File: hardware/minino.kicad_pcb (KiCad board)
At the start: 2 copper layers, 80 x 107.5 mm, 54 parts, among them J1 OLED, J2 GPS, J3 Battery, J5 Micro_SD_Card_Det, P1 USB_C_Plug_USB2.0, Q1 DMG3415U-7, Q2 MMBT2222A, SW1 ON, SW2 LEFT, SW3 RIGTH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

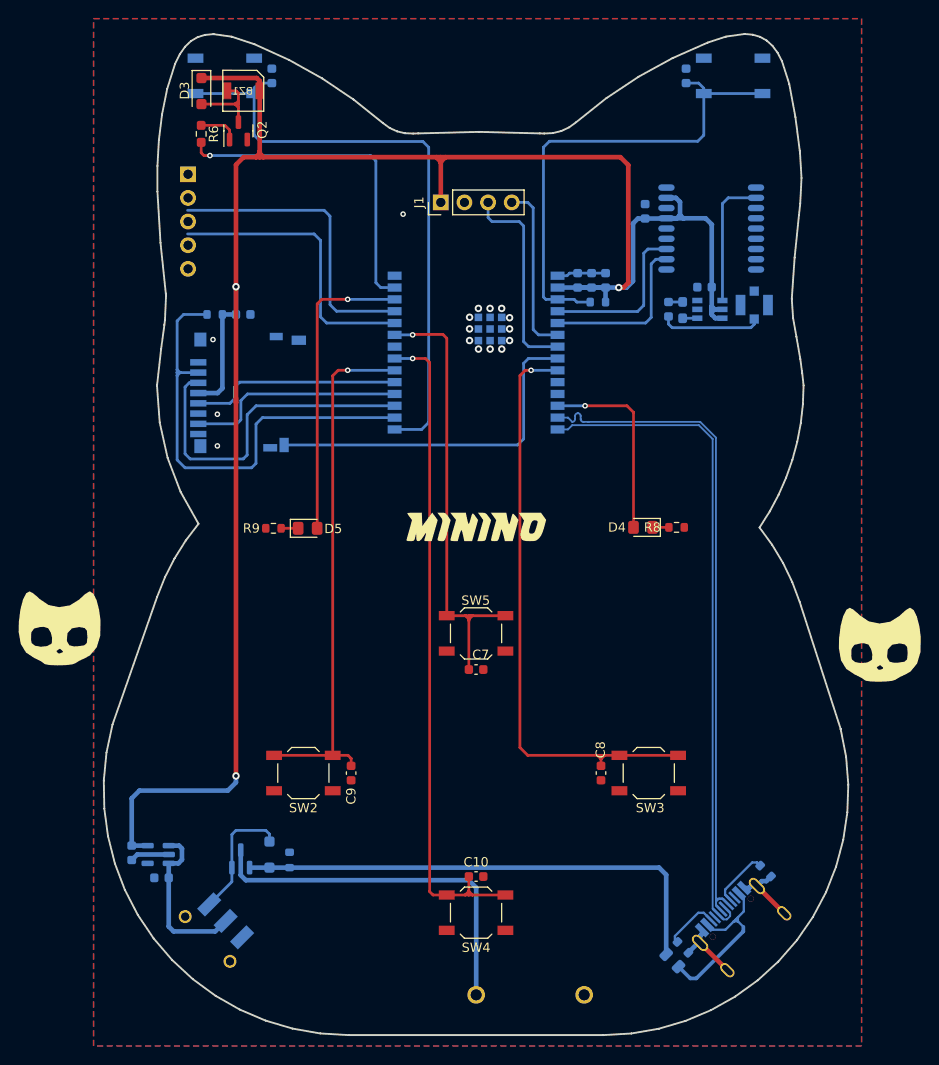
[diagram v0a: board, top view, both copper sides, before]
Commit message: Uart header placed
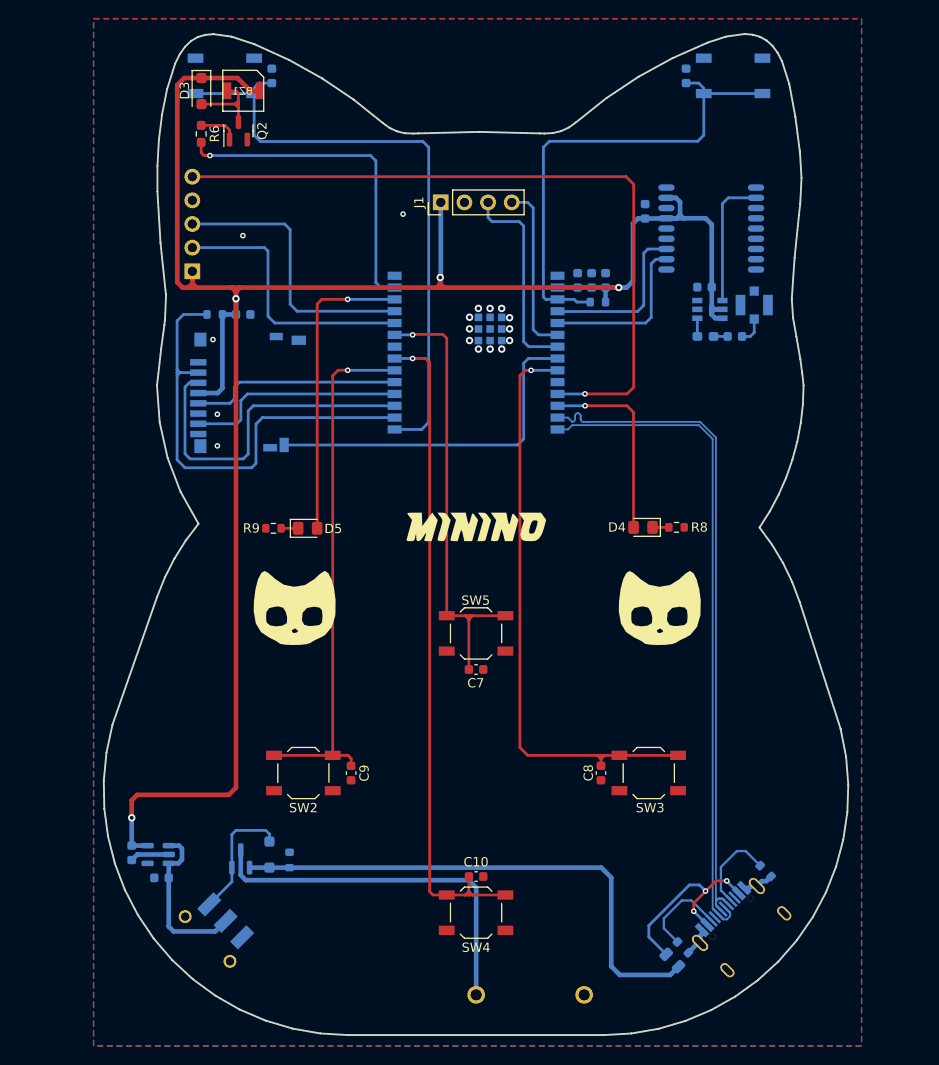
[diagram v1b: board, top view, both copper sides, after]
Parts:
- moved G*** 25.3 mm to (71.2, 83.1)
- moved G*** 24.0 mm to (110.4, 83.1)
- moved J2 10.4 mm to (60.3, 46.9), turned to 0 degrees
- moved C1 7.71 mm to (118.6, 53.9), turned to 0 degrees
- moved L1 3.75 mm to (115.4, 53.9), turned to 0 degrees
- moved G*** 0.59 mm to (72.1, 37.1)
- moved G*** 0.59 mm to (72.7, 45.9)
- turned F1 to -45 degrees
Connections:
- J2 pad 2: /TX -> /RX
- J2 pad 3: /RX -> /TX
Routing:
- net /DIO11: track 0.00 -> 78.0 mm, vias 0 -> 1
- net GND: track 24.4 -> 10.8 mm, vias 16 -> 17
- net Net-(AE1-A): track 10.9 -> 2.93 mm
- net Net-(P1-VCONN): track 6.06 -> 9.94 mm
- net VBUS: track 53.6 -> 56.8 mm
- net Net-(P1-CC): track 6.59 -> 9.66 mm
- net Net-(F1-Pad1): track 19.3 -> 21.4 mm, vias 0 -> 3
- net /TX: track 32.3 -> 30.3 mm
- net /RX: track 31.0 -> 29.2 mm
- net +3V3: track 226.2 -> 226.1 mm, vias 3 -> 4

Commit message: I2C header added
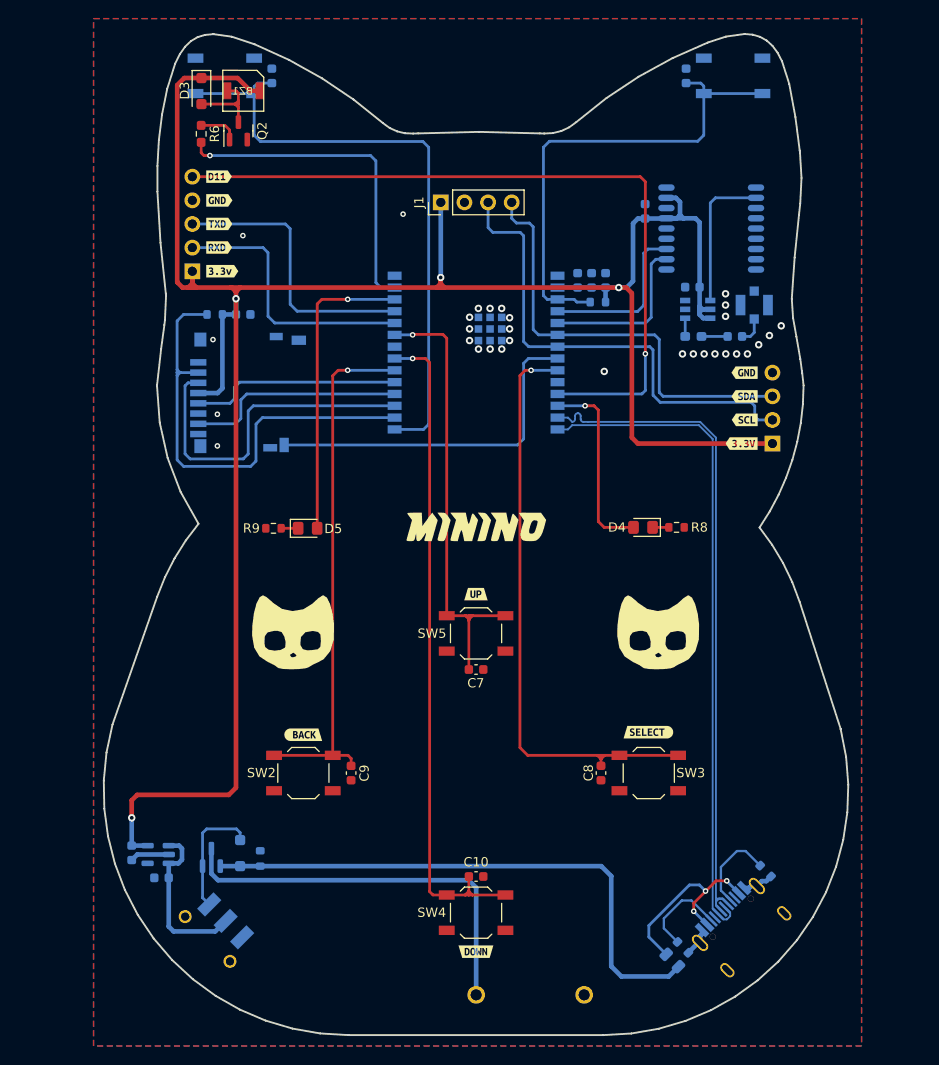
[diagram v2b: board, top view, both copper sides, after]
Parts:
- added J4: I2C, Connector_PinHeader_2.54mm:PinHeader_1x04_P2.54mm_Vertical, B.Cu at (122.6, 65.4)
- added kibuzzard-65BBE191: G***, kibuzzard-65BBE191, F.Cu at (63.2, 36.7)
- added kibuzzard-65BBE1AA: G***, kibuzzard-65BBE1AA, F.Cu at (63.2, 39.3)
- added kibuzzard-65BBE1C5: G***, kibuzzard-65BBE1C5, F.Cu at (63.2, 41.8)
- added kibuzzard-65BBE1CF: G***, kibuzzard-65BBE1CF, F.Cu at (63.2, 44.3)
- added kibuzzard-65BBE243: G***, kibuzzard-65BBE243, F.Cu at (119.6, 57.8)
- added kibuzzard-65BBE252: G***, kibuzzard-65BBE252, F.Cu at (119.6, 60.3)
- added kibuzzard-65BBE261: G***, kibuzzard-65BBE261, F.Cu at (119.6, 62.9)
- added kibuzzard-65BBE26E: G***, kibuzzard-65BBE26E, F.Cu at (119.3, 65.4)
- added kibuzzard-65BBE292: G***, kibuzzard-65BBE292, F.Cu at (63.5, 46.9)
- added kibuzzard-65BBE46A: G***, kibuzzard-65BBE46A, F.Cu at (90.8, 81.6)
- added kibuzzard-65BBE4AF: G***, kibuzzard-65BBE4AF, F.Cu at (90.8, 120.0)
- added kibuzzard-65BBE4ED: G***, kibuzzard-65BBE4ED, F.Cu at (72.2, 96.7)
- added kibuzzard-65BBE507: G***, kibuzzard-65BBE507, F.Cu at (109.3, 96.4)
- AE1: value Antenna -> Antenna_Shield
- J2: value GPS -> UART
- moved Q1 3.15 mm to (62.4, 109.8)
- moved D2 3.15 mm to (65.4, 109.4)
- moved R5 3.15 mm to (67.6, 110.0)
- moved G*** 2.61 mm to (110.2, 85.7)
- moved G*** 2.61 mm to (71.0, 85.7)
- moved U2 1.31 mm to (114.6, 51.0)
- moved C15 1.31 mm to (114.0, 48.6)
- moved L1 1.31 mm to (114.1, 53.9)
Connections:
- AE1 pad 2: (no net) -> GND
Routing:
- net +3V3: track 226.1 -> 257.5 mm
- net /SCL: track 22.1 -> 52.7 mm
- net /SDA: track 18.5 -> 47.4 mm
- net VBUS: track 56.8 -> 60.2 mm
- net +BATT: track 40.0 -> 43.3 mm
- net /DIO11: track 78.0 -> 80.9 mm
- net Net-(U1-RF_IN): track 14.3 -> 15.6 mm
- net Net-(C1-Pad1): track 1.50 -> 2.81 mm
- net Net-(D2-K): track 13.7 -> 13.2 mm
- net GND: vias 17 -> 31

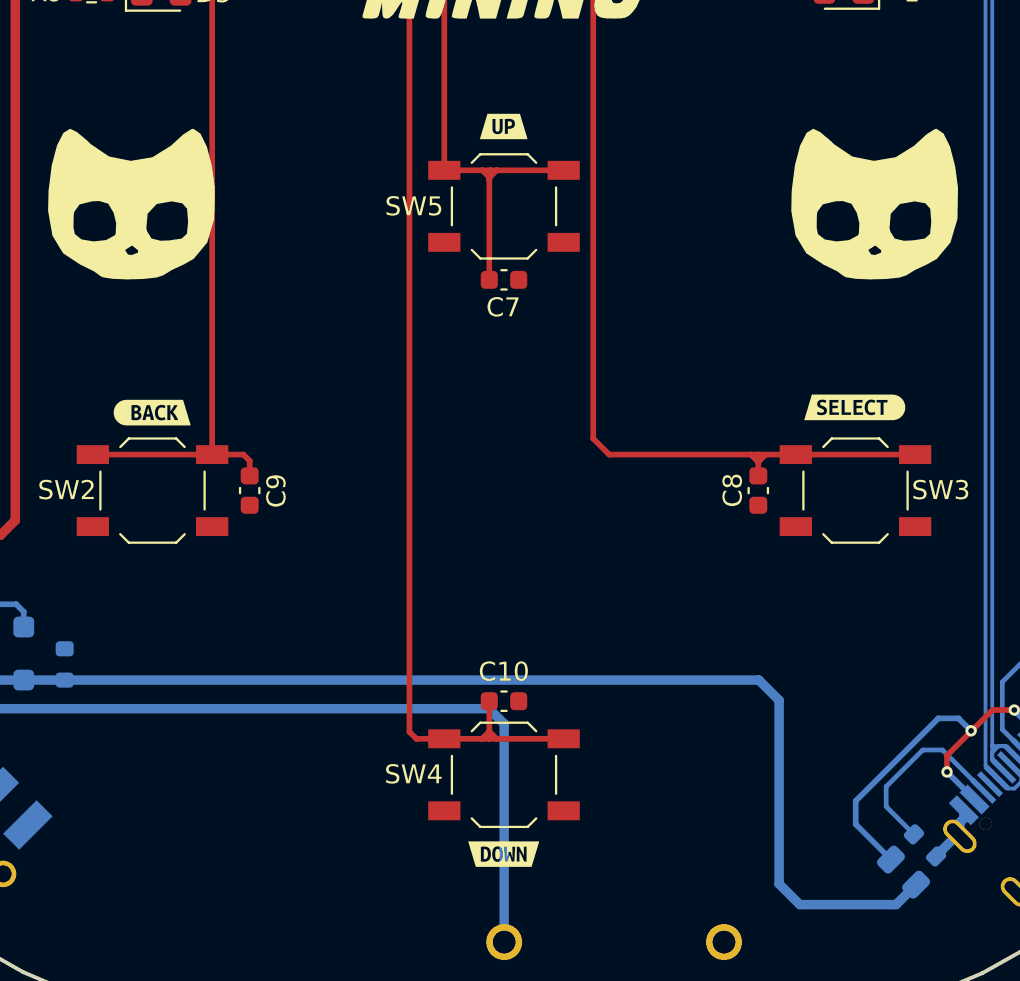
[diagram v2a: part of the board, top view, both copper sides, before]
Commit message: Antenna shielded
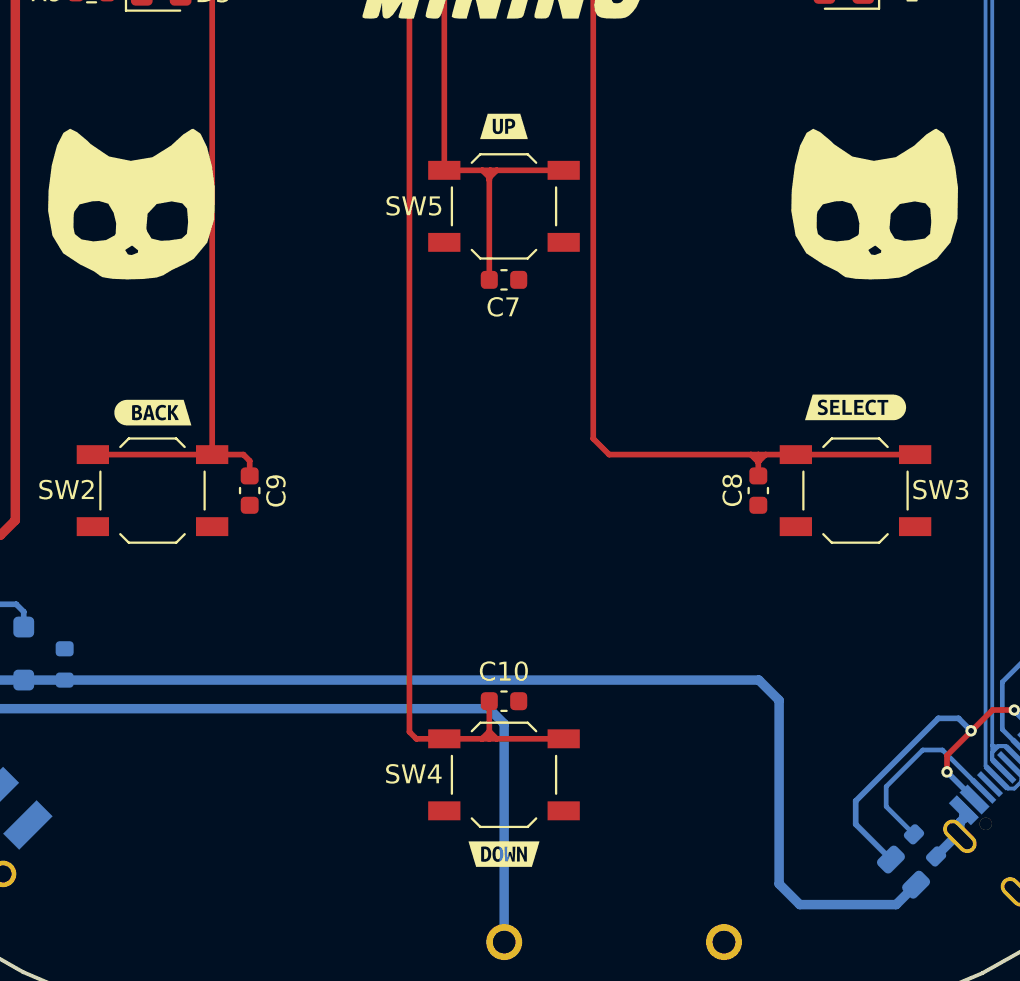
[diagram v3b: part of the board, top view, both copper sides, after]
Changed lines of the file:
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@@
   )
   (footprint "kibuzzard-65BBE4ED" (layer "F.Cu")
-    (at 72.225 96.675)
+    (at 72.258 96.675)
     (descr "Generated with KiBuzzard")
     (tags "kb_params=eyJBbGlnbm1lbnRDaG9pY2UiOiAiQ2VudGVyIiwgIkNhcExlZnRDaG9pY2UiOiAiKCIsICJDYXBSaWdodENob2ljZSI6ICJcXCIsICJGb250Q29tYm9Cb3giOiAiVWJ1bnR1TW9uby1CIiwgIkhlaWdodEN0cmwiOiAiMC44IiwgIkxheWVyQ29tYm9Cb3giOiAiRi5TaWxrUyIsICJNdWx0aUxpbmVUZXh0IjogIkJBQ0siLCAiUGFkZGluZ0JvdHRvbUN0cmwiOiAiNSIsICJQYWRkaW5nTGVmdEN0cmwiOiAiNSIsICJQYWRkaW5nUmlnaHRDdHJsIjogIjUiLCAiUGFkZGluZ1RvcEN0cmwiOiAiNSIsICJXaWR0aEN0cmwiOiAiMC44In0=")
@@
   )
   (footprint "kibuzzard-65BBE46A" (layer "F.Cu")
-    (at 90.775 81.575)
+    (at 90.79 81.57)
     (descr "Generated with KiBuzzard")
     (tags "kb_params=eyJBbGlnbm1lbnRDaG9pY2UiOiAiQ2VudGVyIiwgIkNhcExlZnRDaG9pY2UiOiAiLyIsICJDYXBSaWdodENob2ljZSI6ICJcXCIsICJGb250Q29tYm9Cb3giOiAiVWJ1bnR1TW9uby1CIiwgIkhlaWdodEN0cmwiOiAiMC44IiwgIkxheWVyQ29tYm9Cb3giOiAiRi5TaWxrUyIsICJNdWx0aUxpbmVUZXh0IjogIlVQIiwgIlBhZGRpbmdCb3R0b21DdHJsIjogIjUiLCAiUGFkZGluZ0xlZnRDdHJsIjogIjUiLCAiUGFkZGluZ1JpZ2h0Q3RybCI6ICI1IiwgIlBhZGRpbmdUb3BDdHJsIjogIjUiLCAiV2lkdGhDdHJsIjogIjAuOCJ9")
@@
   )
   (footprint "kibuzzard-65BBE4AF" (layer "F.Cu")
-    (at 90.775 119.975)
+    (at 90.79 119.975)
     (descr "Generated with KiBuzzard")
     (tags "kb_params=eyJBbGlnbm1lbnRDaG9pY2UiOiAiQ2VudGVyIiwgIkNhcExlZnRDaG9pY2UiOiAiXFwiLCAiQ2FwUmlnaHRDaG9pY2UiOiAiLyIsICJGb250Q29tYm9Cb3giOiAiVWJ1bnR1TW9uby1CIiwgIkhlaWdodEN0cmwiOiAiMC44IiwgIkxheWVyQ29tYm9Cb3giOiAiRi5TaWxrUyIsICJNdWx0aUxpbmVUZXh0IjogIkRPV04iLCAiUGFkZGluZ0JvdHRvbUN0cmwiOiAiNSIsICJQYWRkaW5nTGVmdEN0cmwiOiAiNSIsICJQYWRkaW5nUmlnaHRDdHJsIjogIjUiLCAiUGFkZGluZ1RvcEN0cmwiOiAiNSIsICJXaWR0aEN0cmwiOiAiMC44In0=")
@@
   )
   (footprint "kibuzzard-65BBE507" (layer "F.Cu")
-    (at 109.3 96.4)
+    (at 109.342 96.4)
     (descr "Generated with KiBuzzard")
     (tags "kb_params=eyJBbGlnbm1lbnRDaG9pY2UiOiAiQ2VudGVyIiwgIkNhcExlZnRDaG9pY2UiOiAiLyIsICJDYXBSaWdodENob2ljZSI6ICIpIiwgIkZvbnRDb21ib0JveCI6ICJVYnVudHVNb25vLUIiLCAiSGVpZ2h0Q3RybCI6ICIwLjgiLCAiTGF5ZXJDb21ib0JveCI6ICJGLlNpbGtTIiwgIk11bHRpTGluZVRleHQiOiAiU0VMRUNUIiwgIlBhZGRpbmdCb3R0b21DdHJsIjogIjUiLCAiUGFkZGluZ0xlZnRDdHJsIjogIjUiLCAiUGFkZGluZ1JpZ2h0Q3RybCI6ICI1IiwgIlBhZGRpbmdUb3BDdHJsIjogIjUiLCAiV2lkdGhDdHJsIjogIjAuOCJ9")

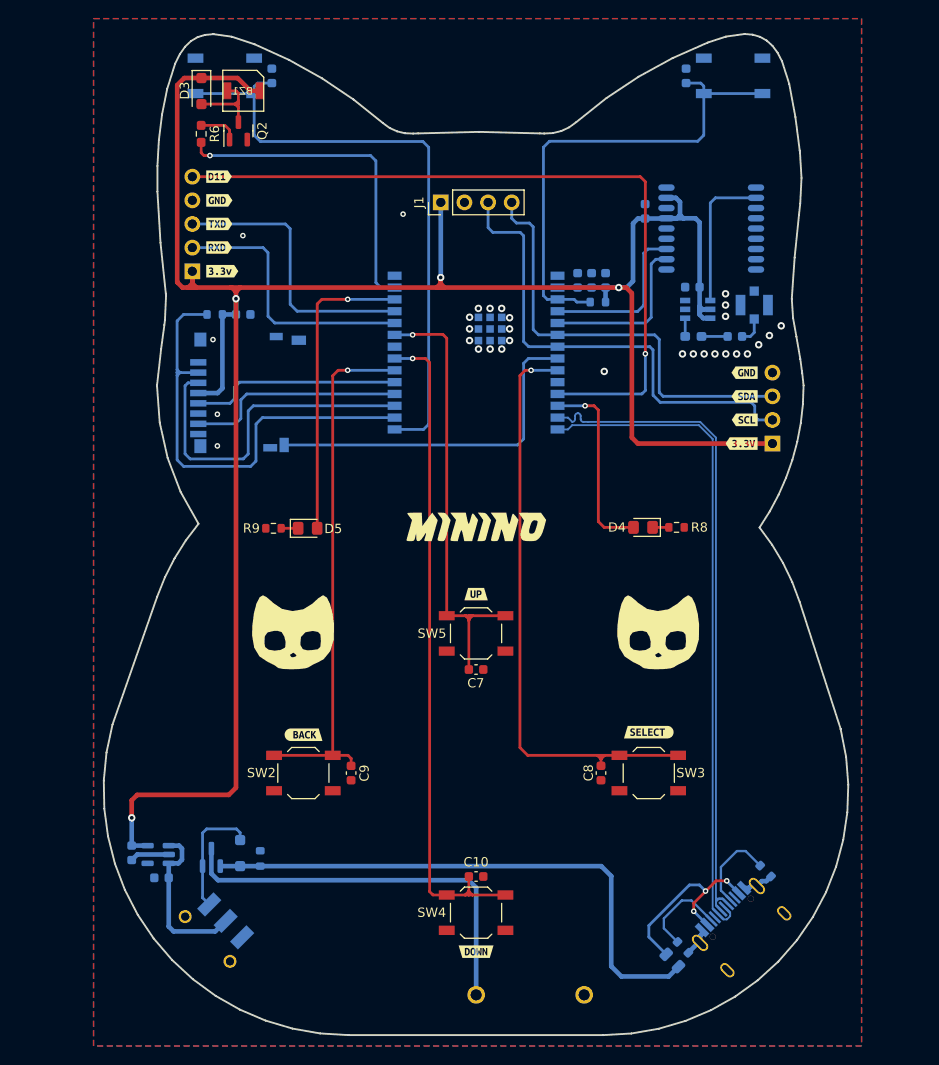
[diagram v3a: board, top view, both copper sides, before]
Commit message: Update_Labels_replace_button_capacitors
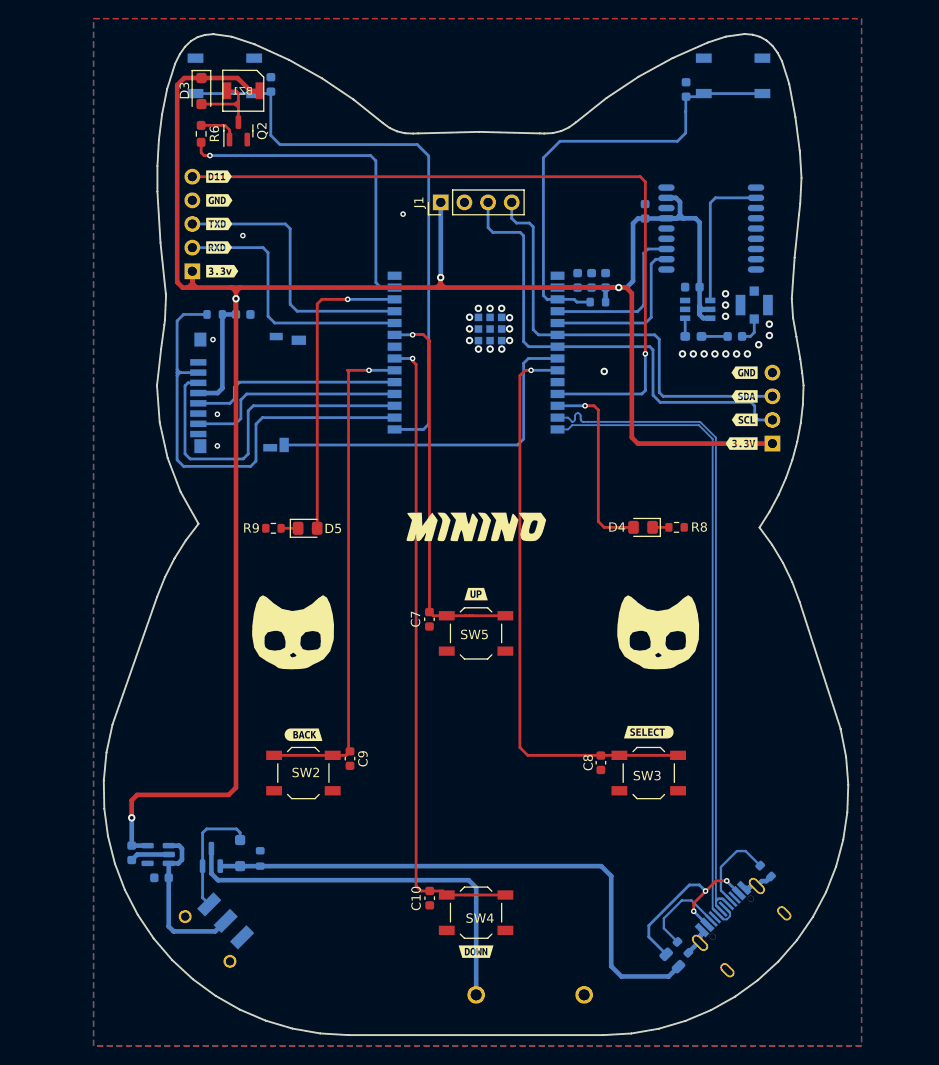
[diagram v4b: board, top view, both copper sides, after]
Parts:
- added kibuzzard-65BC2610: G***, kibuzzard-65BC2610, B.Cu at (65.4, 113.3)
- added kibuzzard-65BC266D: G***, kibuzzard-65BC266D, B.Cu at (70.2, 118.2)
- added kibuzzard-65BC2810: G***, kibuzzard-65BC2810, B.Cu at (118.4, 30.1)
- added kibuzzard-65BC2821: G***, kibuzzard-65BC2821, B.Cu at (63.6, 30.2)
- moved C7 7.36 mm to (85.8, 84.3), turned to 90 degrees
- moved C10 5.50 mm to (85.8, 114.2), turned to 90 degrees
- moved C9 1.55 mm to (77.2, 99.2)
- moved C11 1.46 mm to (113.3, 27.4)
- moved C8 1.11 mm to (104.2, 99.7)
- moved C12 0.93 mm to (68.8, 26.8)
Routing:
- net /UP: track 48.9 -> 41.5 mm
- net /EN: track 52.6 -> 48.8 mm
- net /DOWN: track 72.1 -> 68.7 mm
- net /BOOT: track 66.5 -> 63.5 mm
- net /SELECT: track 63.8 -> 60.8 mm
- net /BACK: track 56.9 -> 54.4 mm
